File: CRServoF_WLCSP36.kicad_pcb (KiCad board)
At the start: 4 copper layers, 17.8 x 19.7 mm, 33 parts, among them J1 Conn_02x06_Counter_Clockwise, J2 Conn_02x06_Counter_Clockwise, J3 Conn_01x03, J4 Conn_01x04, J5 Conn_01x03, U1 TPS727xxDSE, U2 STM32F051T8Yx

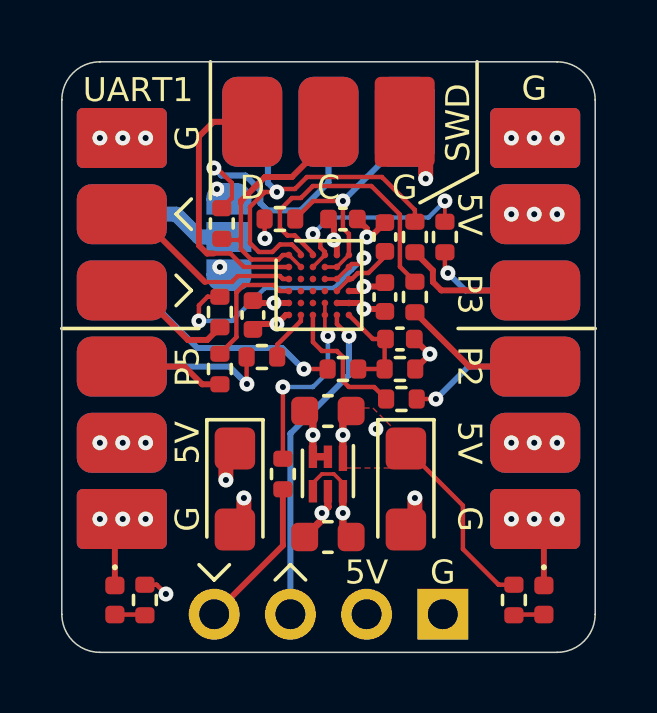
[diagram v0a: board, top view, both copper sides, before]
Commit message: update schematic and silk screen
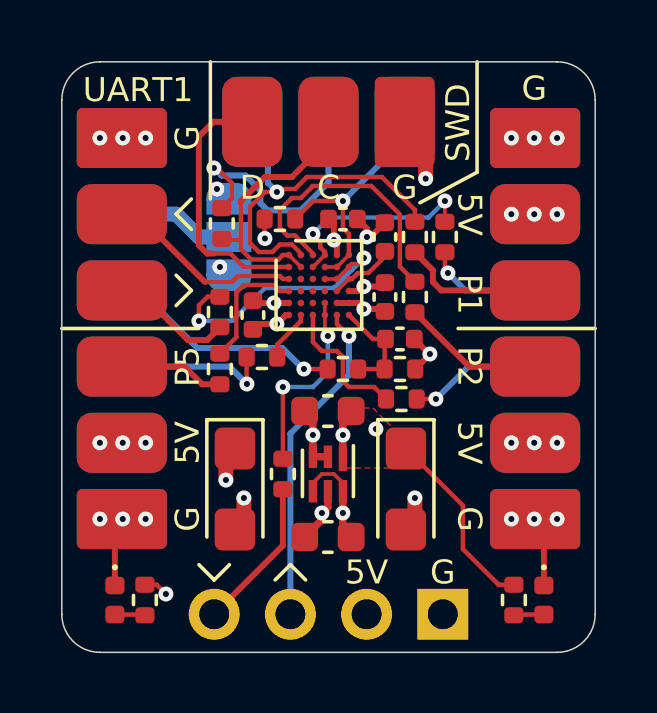
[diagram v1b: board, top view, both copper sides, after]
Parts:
- U1: value TPS727xxDSE -> TPS72733DSE
